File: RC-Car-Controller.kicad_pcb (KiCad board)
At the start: 4 copper layers, 140 x 6 mm, 92 parts, among them J1 USB_C_Receptacle_USB2.0, J2 Power_Input, J3 Conn_01x11_Socket, J4 MOTOR_1_OUTPUT, J5 MOTOR_2_OUTPUT, J6 MOTOR_3_OUTPUT, J7 MOTOR_4_OUTPUT, J9 Conn_01x11_Socket, SW2 SW_Push, SW4 SW_Push, U1 LMR14020SDDAR, U10 DRV8874PWPR, U11 DRV8874PWPR, U2 SPX3819M5-L-3-3, U3 USBLC6-2SC6, U4 BMI055, U5 DRV8874PWPR, U6 W25Q32JVSS, U8 ESP32-S3, U9 DRV8874PWPR, X2 40MHz

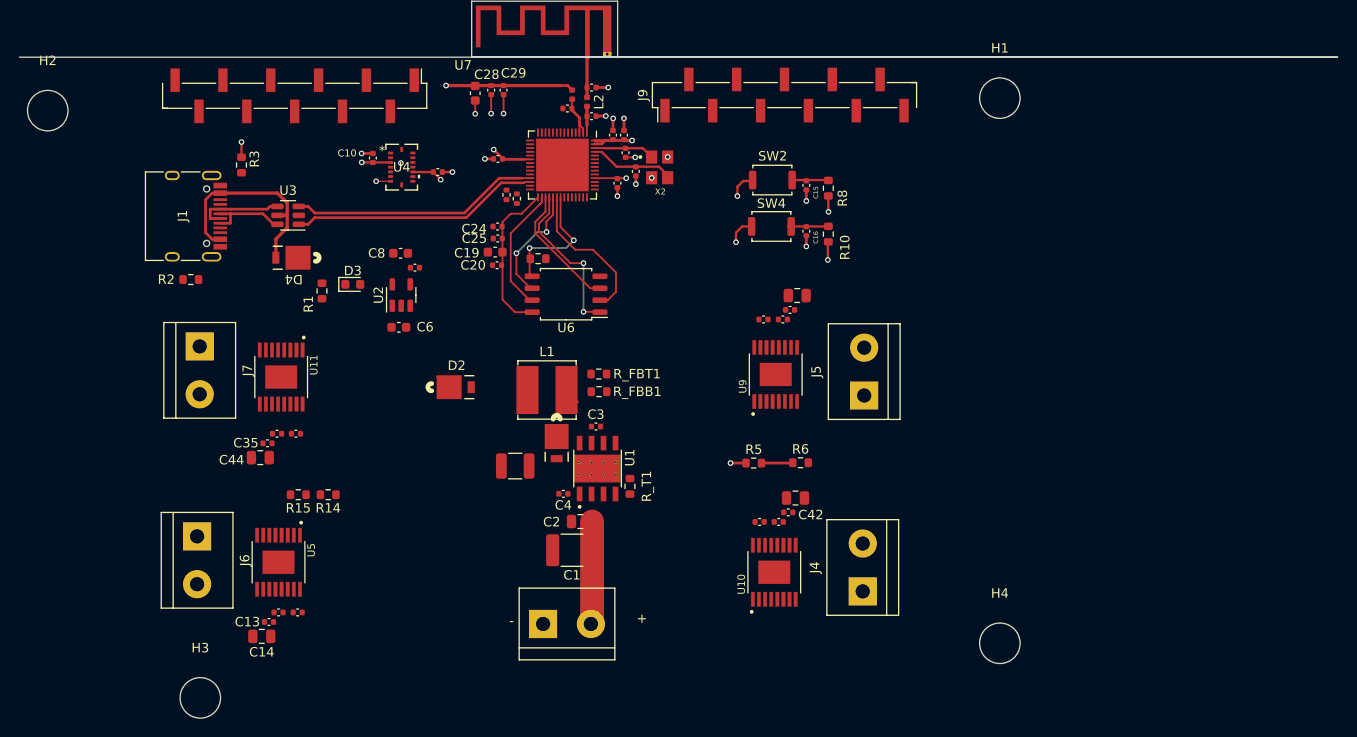
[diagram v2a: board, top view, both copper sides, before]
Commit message: add libraries folder
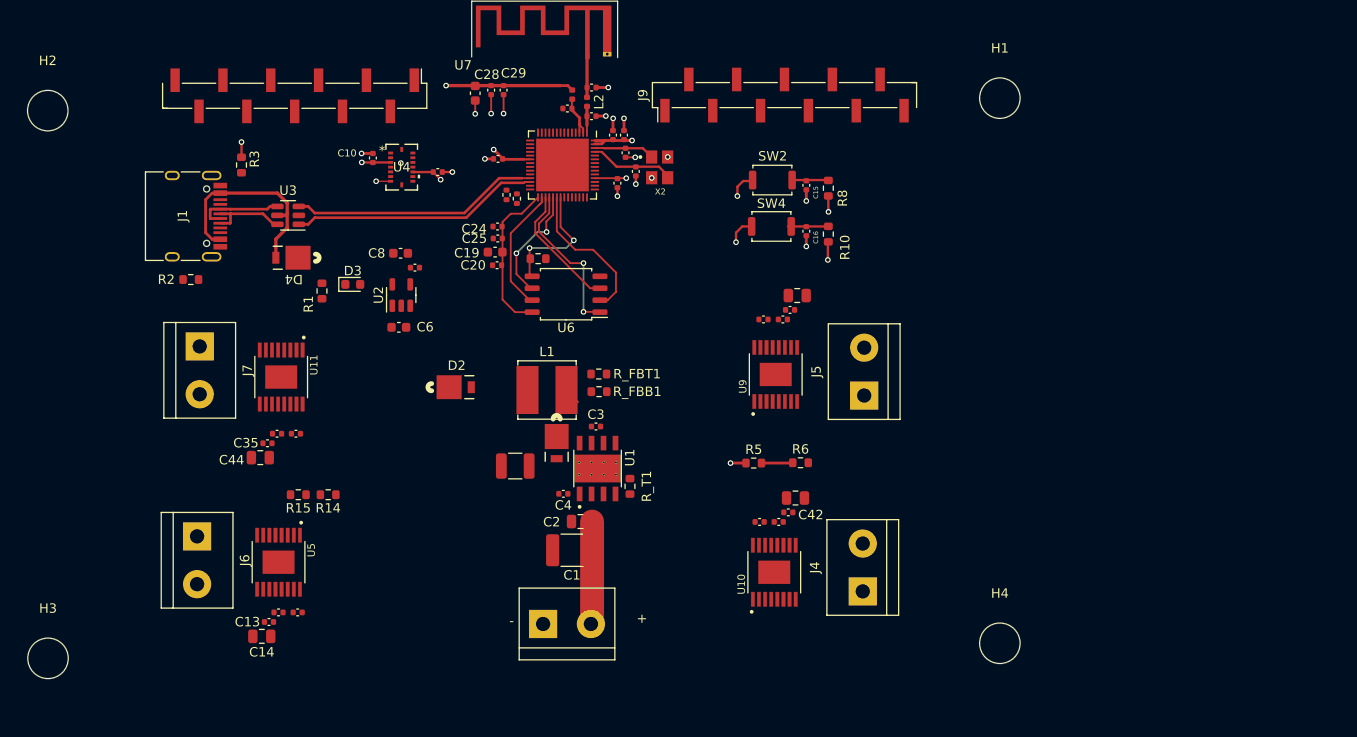
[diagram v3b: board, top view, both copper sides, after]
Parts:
- moved H3 16.7 mm to (88.9, 101.6)
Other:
- board size 140 x 6 mm -> 15.5 x 6 mm
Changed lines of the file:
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@@
   )
   (footprint "MountingHole:MountingHole_4.3mm_M4" (layer "F.Cu")
-    (at 105.075 105.8)
+    (at 88.9 101.6)
     (descr "Mounting Hole 4.3mm, no annular, M4")
     (tags "mounting hole 4.3mm no annular m4")
@@
     )
   )
-  (gr_line (start 133.9 37.725) (end 225.875 37.75)
-    (stroke (width 0.1) (type default)) (layer "Edge.Cuts"))
   (gr_line (start 133.9 37.725) (end 133.9 31.8)
     (stroke (width 0.1) (type default)) (layer "Edge.Cuts"))
-  (gr_line (start 225.875 37.75) (end 85.85 37.75)
-    (stroke (width 0.1) (type default)) (layer "Edge.Cuts"))
   (gr_line (start 149.4 31.8) (end 149.4 37.8)

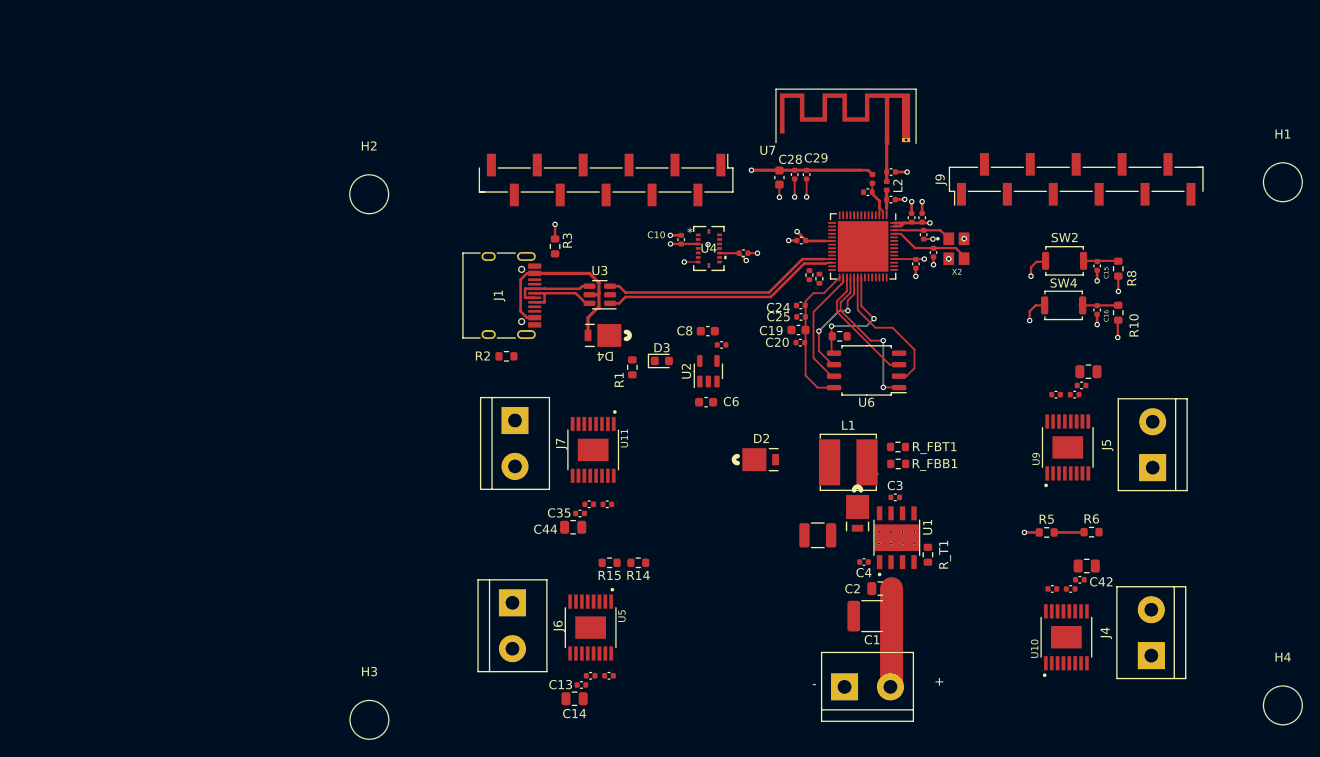
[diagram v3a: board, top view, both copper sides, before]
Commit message: Align mounting holes + edge cuts
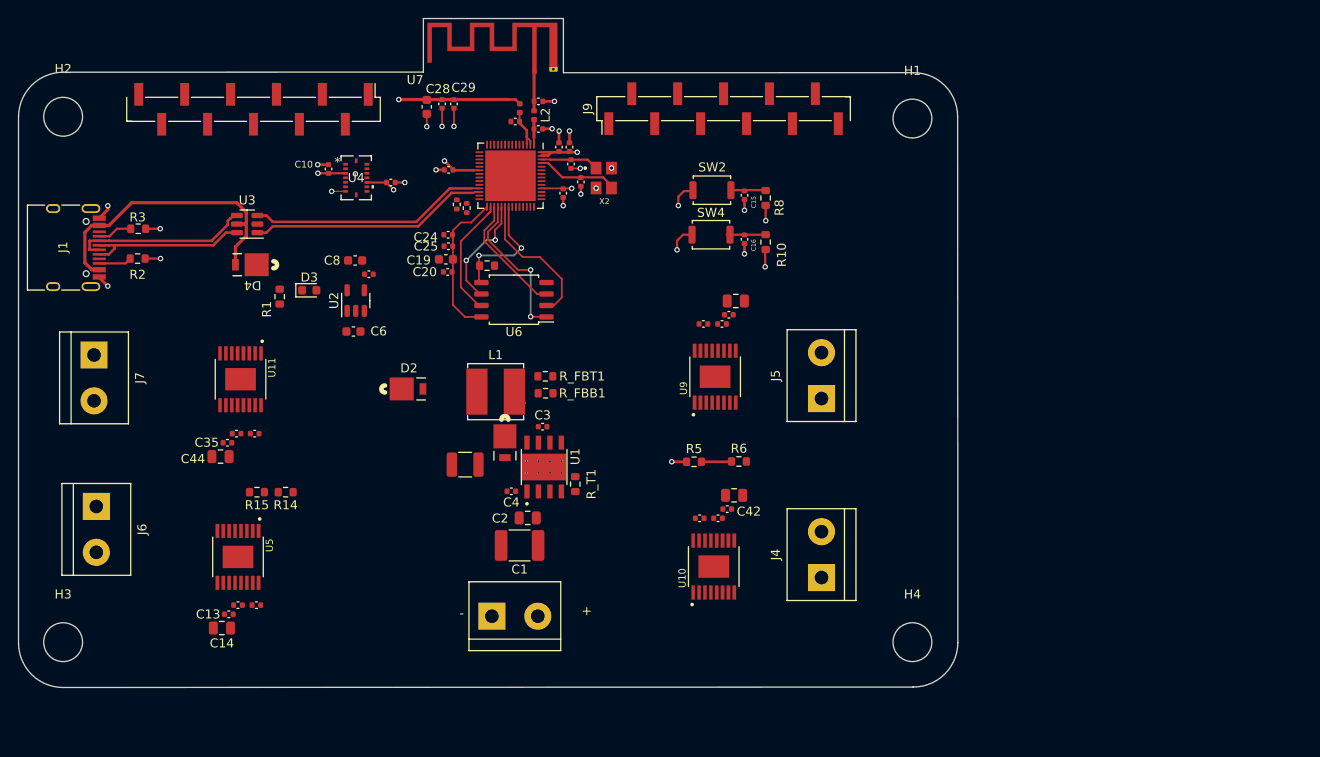
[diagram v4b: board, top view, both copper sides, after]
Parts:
- moved J1 48.5 mm to (55.0, 49.3)
- moved J6 47.3 mm to (58.7, 78.0)
- moved J7 47.2 mm to (58.4, 61.2)
- moved R3 46.2 mm to (63.3, 47.2), turned to 0 degrees
- moved R2 42.2 mm to (63.2, 50.5), turned to 0 degrees
- moved H1 41.6 mm to (149.0, 35.1)
- moved H4 41.6 mm to (149.0, 93.0)
- moved C21 39.8 mm to (107.6, 36.2)
- moved C24 39.8 mm to (97.6, 47.9)
- moved C26 39.8 mm to (111.2, 40.1)
- moved C36 39.8 mm to (125.9, 57.8)
- moved C9 39.8 mm to (91.3, 42.1)
- moved D1 39.8 mm to (103.9, 70.9)
- moved J2 39.8 mm to (102.5, 90.1)
- moved R_FBB1 39.8 mm to (108.4, 65.5)
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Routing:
- net +36V: track 10.9 -> 0.18 mm
- net /Connectors/C_D-: track 9.32 -> 19.8 mm
- net +VBUS: track 22.2 -> 32.4 mm
- net /Connectors/C_D+: track 8.61 -> 18.2 mm
- net GND: track 25.8 -> 30.7 mm, vias 21 -> 24
- net Net-(J1-CC1): track 0.00 -> 3.83 mm
- net Net-(J1-CC2): track 0.00 -> 3.65 mm
- added copper zone on In1.Cu, net GND
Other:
- board size 15.5 x 6 mm -> 104 x 74 mm

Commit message: route motors
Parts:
- added J8: Conn_01x03_Socket, Connector_PinSocket_2.54mm:PinSocket_1x03_P2.54mm_Vertical, F.Cu at (85.2, 71.0)
- moved J4 5.26 mm to (143.9, 84.0)
- moved J5 4.98 mm to (143.9, 66.2)
- moved R5 3.74 mm to (127.9, 71.0)
- moved R6 3.62 mm to (129.6, 69.4)
- moved U9 1.70 mm to (128.3, 62.4)
- moved C38 1.67 mm to (129.8, 55.6)
- moved C36 1.53 mm to (126.8, 56.6)
- moved C37 1.53 mm to (128.9, 56.6)
- moved C39 1.53 mm to (130.4, 54.0)
- moved C15 1.34 mm to (131.5, 42.8)
- moved C16 1.34 mm to (131.5, 47.7)
- moved SW2 1.34 mm to (127.9, 42.3)
- moved SW4 1.34 mm to (127.8, 47.2)
- moved R10 1.34 mm to (133.9, 48.0)
- moved R8 1.34 mm to (133.9, 43.1)
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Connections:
- U10 pad 17: (no net) -> GND
- U11 pad 17: (no net) -> GND
- U5 pad 17: (no net) -> GND
- U9 pad 17: (no net) -> GND
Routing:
- net GND: track 30.7 -> 82.1 mm, vias 24 -> 50
- net MOTOR_2_OUT_2: track 0.00 -> 17.8 mm
- net +36V: track 0.18 -> 15.7 mm, vias 0 -> 12
- net MOTOR_2_OUT_1: track 0.00 -> 13.7 mm
- net Net-(U9-CPL): track 0.00 -> 3.41 mm
- net Net-(U9-CPH): track 0.00 -> 3.28 mm
- net Net-(U9-VCP): track 0.00 -> 3.09 mm
- net Net-(U10-CPL): track 0.00 -> 2.99 mm
- net Net-(U5-CPL): track 0.00 -> 2.94 mm
- net +3V3: track 39.7 -> 42.6 mm, vias 10 -> 11
- net Net-(U10-CPH): track 0.00 -> 2.86 mm
- net Net-(U5-CPH): track 0.00 -> 2.81 mm
- net Net-(U5-VCP): track 0.00 -> 2.71 mm
- net Net-(U10-VCP): track 0.00 -> 2.70 mm
- net /ESP32-S3 Microcontroller /RESET: track 3.93 -> 5.85 mm, vias 0 -> 1
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- added copper zone on B.Cu, net +36V
- added copper zone on F.Cu, net +36V
- added copper zone on F.Cu, net GND

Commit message: before changing motors
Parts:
- moved C20 2.79 mm to (97.7, 54.8)
- moved C19 2.68 mm to (97.4, 53.3)
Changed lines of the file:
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@@
     )
     (pad_to_mask_clearance 0)
-    (aux_axis_origin 48.768 99.314)
+    (aux_axis_origin 149.098 93.0402)
     (pcbplotparams
       (layerselection 0x00010fc_ffffffff)
@@
   )
   (footprint "Capacitor_SMD:C_0402_1005Metric" (layer "F.Cu")
-    (at 97.565 52.028 180)
+    (at 97.663 54.8132 180)
     (descr "Capacitor SMD 0402 (1005 Metric), square (rectangular) end terminal, IPC_7351 nominal, (Body size source: IPC-SM-782 page 76, https://www.pcb-3d.com/wordpress/wp-content/uploads/ipc-sm-782a_amendment_1_and_2.pdf), generated with kicad-footprint-generator")
     (tags "capacitor")
@@
   )
   (footprint "Capacitor_SMD:C_0603_1608Metric" (layer "F.Cu")
-    (at 97.3618 50.631 180)
+    (at 97.3836 53.3146 180)
     (descr "Capacitor SMD 0603 (1608 Metric), square (rectangular) end terminal, IPC_7351 nominal, (Body size source: IPC-SM-782 page 76, https://www.pcb-3d.com/wordpress/wp-content/uploads/ipc-sm-782a_amendment_1_and_2.pdf), generated with kicad-footprint-generator")
     (tags "capacitor")
@@
   (segment (start 75.095 46.728) (end 74.2325 46.728) (width 0.3556) (layer "F.Cu") (net 9))
   (segment (start 75.2728 48.046622) (end 75.2728 46.5502) (width 0.3556) (layer "F.Cu") (net 9))
-  (segment (start 57.4062 51.00958) (end 58.17462 51.778) (width 0.3556) (layer "F.Cu") (net 9))
-  (segment (start 57.4062 47.64642) (end 57.4062 51.00958) (width 0.3556) (layer "F.Cu") (net 9))
-  (segment (start 74.226822 44.3634) (end 62.5902 44.3634) (width 0.3556) (layer "F.Cu") (net 9))
-  (segment (start 75.2728 45.409378) (end 74.226822 44.3634) (width 0.3556) (layer "F.Cu") (net 9))
-  (segment (start 75.2728 46.5502) (end 75.095 46.728) (width 0.3556) (layer "F.Cu") (net 9))
+  (segment (start 75.2728 46.5502) (end 75.2728 45.405222) (width 0.3556) (layer "F.Cu") (net 9))
   (segment (start 60.0756 46.878) (end 58.995 46.878) (width 0.3556) (layer "F.Cu") (net 9))
-  (segment (start 62.5902 44.3634) (end 60.0756 46.878) (width 0.3556) (layer "F.Cu") (net 9))
+  (segment (start 75.2728 46.5502) (end 75.095 46.728) (width 0.3556) (layer "F.Cu") (net 9))
+  (segment (start 58.995 46.878) (end 58.17462 46.878) (width 0.3556) (layer "F.Cu") (net 9))
+  (segment (start 57.0738 47.97882) (end 57.0738 50.67718) (width 0.3556) (layer "F.Cu") (net 9))
   (segment (start 74.07 49.249422) (end 75.2728 48.046622) (width 0.3556) (layer "F.Cu") (net 9))
-  (segment (start 75.2728 46.5502) (end 75.2728 45.409378) (width 0.3556) (layer "F.Cu") (net 9))
-  (segment (start 74.07 51.228) (end 74.07 49.249422) (width 0.3556) (layer "F.Cu") (net 9))
-  (segment (start 58.17462 46.878) (end 57.4062 47.64642) (width 0.3556) (layer "F.Cu") (net 9))
+  (segment (start 62.3766 44.577) (end 60.0756 46.878) (width 0.3556) (layer "F.Cu") (net 9))
+  (segment (start 57.0738 50.67718) (end 58.17462 51.778) (width 0.3556) (layer "F.Cu") (net 9))
   (segment (start 58.17462 51.778) (end 58.995 51.778) (width 0.3556) (layer "F.Cu") (net 9))
-  (segment (start 58.995 46.878) (end 58.17462 46.878) (width 0.3556) (layer "F.Cu") (net 9))
+  (segment (start 74.444578 44.577) (end 62.3766 44.577) (width 0.3556) (layer "F.Cu") (net 9))
+  (segment (start 74.07 51.228) (end 74.07 49.249422) (width 0.3556) (layer "F.Cu") (net 9))
+  (segment (start 75.2728 45.405222) (end 74.444578 44.577) (width 0.3556) (layer "F.Cu") (net 9))
+  (segment (start 58.17462 46.878) (end 57.0738 47.97882) (width 0.3556) (layer "F.Cu") (net 9))
   (segment (start 78.206651 46.4834) (end 77.501251 45.778) (width 0.286) (layer "F.Cu") (net 10))
   (segment (start 100.227 42.7782) (end 100.22 42.7852) (width 0.2) (layer "F.Cu") (net 10))
@@
   (segment (start 58.995 49.078) (end 60.082501 49.078) (width 0.286) (layer "F.Cu") (net 31))
   (segment (start 60.706 49.0726) (end 71.629734 49.0726) (width 0.286) (layer "F.Cu") (net 31))
-  (segment (start 57.927 48.585) (end 57.934 48.578) (width 0.286) (layer "F.Cu") (net 32))
+  (segment (start 57.5946 48.9174) (end 57.934 48.578) (width 0.286) (layer "F.Cu") (net 32))
   (segment (start 60.087901 48.5834) (end 71.4271 48.5834) (width 0.286) (layer "F.Cu") (net 32))
-  (segment (start 58.995 49.578) (end 57.934 49.578) (width 0.286) (layer "F.Cu") (net 32))
   (segment (start 73.549 46.085) (end 73.856 45.778) (width 0.286) (layer "F.Cu") (net 32))
-  (segment (start 57.927 49.571) (end 57.927 48.585) (width 0.286) (layer "F.Cu") (net 32))
+  (segment (start 57.934 48.578) (end 58.995 48.578) (width 0.286) (layer "F.Cu") (net 32))
   (segment (start 73.227 46.7835) (end 73.227 46.369636) (width 0.286) (layer "F.Cu") (net 32))
   (segment (start 73.856 45.778) (end 74.2325 45.778) (width 0.286) (layer "F.Cu") (net 32))
   (segment (start 60.082501 48.578) (end 60.087901 48.5834) (width 0.286) (layer "F.Cu") (net 32))
   (segment (start 73.511636 46.085) (end 73.549 46.085) (width 0.286) (layer "F.Cu") (net 32))
-  (segment (start 57.934 48.578) (end 58.995 48.578) (width 0.286) (layer "F.Cu") (net 32))
+  (segment (start 57.5946 49.2386) (end 57.5946 48.9174) (width 0.286) (layer "F.Cu") (net 32))
+  (segment (start 58.995 49.578) (end 57.934 49.578) (width 0.286) (layer "F.Cu") (net 32))
   (segment (start 58.995 48.578) (end 60.082501 48.578) (width 0.286) (layer "F.Cu") (net 32))
   (segment (start 73.227 46.369636) (end 73.511636 46.085) (width 0.286) (layer "F.Cu") (net 32))
-  (segment (start 57.934 49.578) (end 57.927 49.571) (width 0.286) (layer "F.Cu") (net 32))
+  (segment (start 57.934 49.578) (end 57.5946 49.2386) (width 0.286) (layer "F.Cu") (net 32))
   (segment (start 71.4271 48.5834) (end 73.227 46.7835) (width 0.286) (layer "F.Cu") (net 32))
   (segment (start 75.3306 88.17564) (end 76.1212 88.96624) (width 0.3556) (layer "F.Cu") (net 34))
